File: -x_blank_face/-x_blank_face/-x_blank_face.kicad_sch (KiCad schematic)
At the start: 29 parts, among them J1 Conn_01x08_Pin, J2 Conn_01x02_Pin, J3 Conn_01x02_Pin

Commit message: I forgot what I changed
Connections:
- net +X Drain: now also J1.5 (Pin_5), J1.6 (Pin_6); no longer J1.3 (Pin_3), J1.4 (Pin_4)
- net -X Serial Out: now also J1.3 (Pin_3), J1.4 (Pin_4); no longer J1.5 (Pin_5), J1.6 (Pin_6)
- net 12VPDM: now also J1.7 (Pin_7), J1.8 (Pin_8); no longer J1.1 (Pin_1), J1.2 (Pin_2)
- net GND: now also J1.1 (Pin_1), J1.2 (Pin_2); no longer J1.7 (Pin_7), J1.8 (Pin_8)
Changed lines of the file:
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@@
+	(wire
+		(pts
+			(xy 33.02 95.25) (xy 49.53 95.25)
+		)
+		(stroke
+			(width 0)
+			(type default)
+		)
+	)
 	(wire
 		(pts
@@
 	(wire
 		(pts
+			(xy 33.02 107.95) (xy 38.1 107.95)
+		)
+		(stroke
+			(width 0)
+			(type default)
+		)
+	)
+	(wire
+		(pts
+			(xy 33.02 110.49) (xy 36.83 110.49)
+		)
+		(stroke
+			(width 0)
+			(type default)
+		)
+	)
+	(wire
+		(pts
 			(xy 31.75 64.77) (xy 35.56 64.77)
 		)
@@
 	(wire
 		(pts
-			(xy 35.56 95.25) (xy 33.02 95.25)
-		)
-		(stroke
-			(width 0)
-			(type default)
-		)
-	)
-	(wire
-		(pts
 			(xy 35.56 58.42) (xy 35.56 64.77)
 		)
@@
 	(wire
 		(pts
-			(xy 38.1 107.95) (xy 33.02 107.95)
+			(xy 33.02 92.71) (xy 53.34 92.71)
 		)
 		(stroke
@@
 		)
 	)
-	(wire
-		(pts
-			(xy 41.91 92.71) (xy 33.02 92.71)
-		)
-		(stroke
-			(width 0)
-			(type default)
-		)
-	)
 	(label "+X Drain"
-		(at 33.02 100.33 0)
+		(at 33.02 102.87 0)
 		(effects
 			(font
@@
 	)
 	(label "+X Drain"
-		(at 33.02 97.79 0)
+		(at 33.02 105.41 0)
 		(effects
 			(font
@@
 	)
 	(label "12VPDM"
-		(at 35.56 95.25 0)
+		(at 36.83 110.49 0)
 		(effects
 			(font
@@
 	)
 	(label "-X Serial Out"
-		(at 33.02 105.41 0)
+		(at 33.02 100.33 0)
 		(effects
 			(font
@@
 	)
 	(label "-X Serial Out"
-		(at 33.02 102.87 0)
+		(at 33.02 97.79 0)
 		(effects
 			(font
@@
 	)
 	(label "12VPDM"
-		(at 41.91 92.71 0)
+		(at 38.1 107.95 0)
 		(effects
 			(font
@@
 	(symbol
 		(lib_id "power:GND")
-		(at 33.02 110.49 0)
+		(at 49.53 95.25 0)
 		(unit 1)
 		(exclude_from_sim no)
@@
 		(dnp no)
 		(property "Reference" "#PWR04"
-			(at 33.02 116.84 0)
+			(at 49.53 101.6 0)
 			(effects
 				(font
@@
 		)
 		(property "Value" "GND"
-			(at 34.036 114.046 0)
+			(at 50.546 98.806 0)
 			(effects
 				(font
@@
 		)
 		(property "Footprint" ""
-			(at 33.02 110.49 0)
+			(at 49.53 95.25 0)
 			(effects
 				(font
@@
 		)
 		(property "Datasheet" ""
-			(at 33.02 110.49 0)
+			(at 49.53 95.25 0)
 			(effects
 				(font
@@
 		)
 		(property "Description" "Power symbol creates a global label with name \"GND\" , ground"
-			(at 33.02 110.49 0)
+			(at 49.53 95.25 0)
 			(effects
 				(font
@@
 	(symbol
 		(lib_id "power:GND")
-		(at 38.1 107.95 0)
+		(at 53.34 92.71 0)
 		(unit 1)
 		(exclude_from_sim no)
@@
 		(dnp no)
 		(property "Reference" "#PWR03"
-			(at 38.1 114.3 0)
+			(at 53.34 99.06 0)
 			(effects
 				(font
@@
 		)
 		(property "Value" "GND"
-			(at 39.878 111.252 0)
+			(at 55.118 96.012 0)
 			(effects
 				(font
@@
 		)
 		(property "Footprint" ""
-			(at 38.1 107.95 0)
+			(at 53.34 92.71 0)
 			(effects
 				(font
@@
 		)
 		(property "Datasheet" ""
-			(at 38.1 107.95 0)
+			(at 53.34 92.71 0)
 			(effects
 				(font
@@
 		)
 		(property "Description" "Power symbol creates a global label with name \"GND\" , ground"
-			(at 38.1 107.95 0)
-			(effects
-				(font
+			(at 53.34 92.71 0)
+			(effects
+				(font

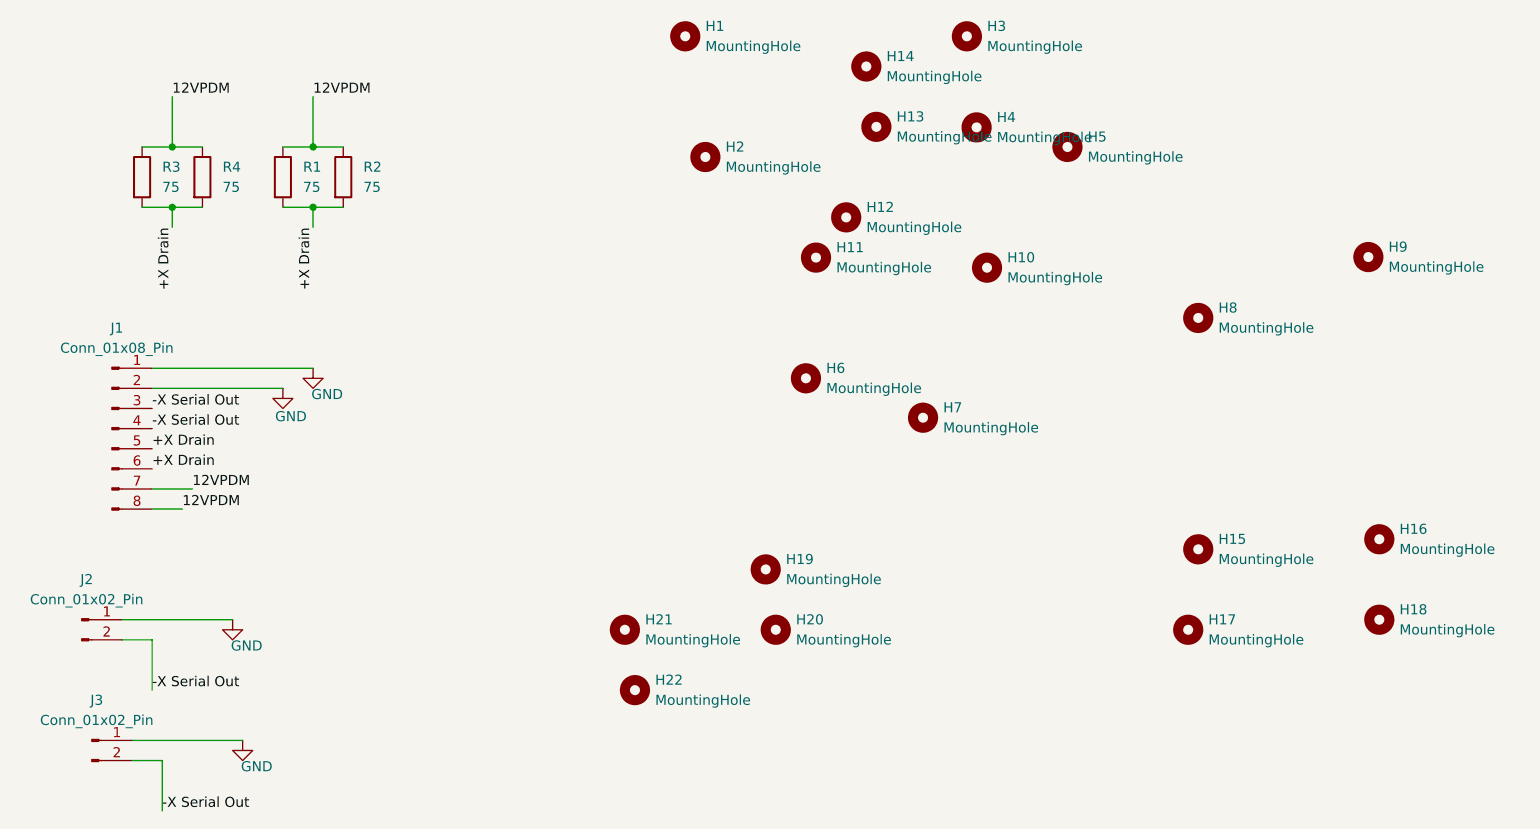
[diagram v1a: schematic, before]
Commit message: Removed GND and PWR plane, replaced with traces, switches are now in series rather than in parallel
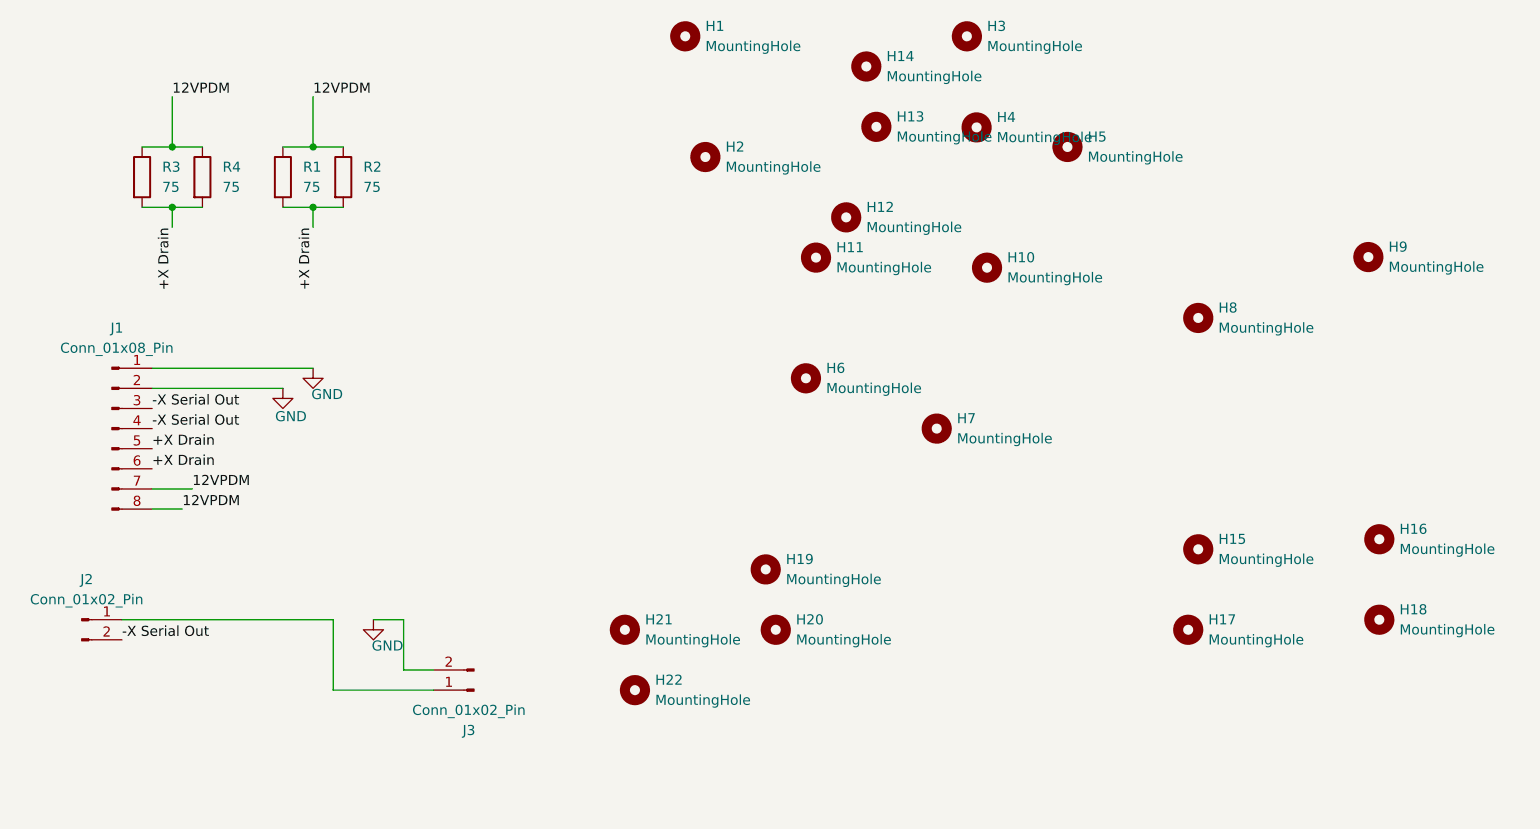
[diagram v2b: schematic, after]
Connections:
- net -X Serial Out: no longer J3.2 (Pin_2)
- net GND: now also J3.2 (Pin_2); no longer J2.1 (Pin_1), J3.1 (Pin_1)
- new net: J2.1 (Pin_1), J3.1 (Pin_1)
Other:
- moved on the sheet: H7, J3
